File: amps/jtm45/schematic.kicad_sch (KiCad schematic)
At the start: 63 parts, among them T3 OT

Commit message: Add: the 56 pF the JTM45 drawing hangs across the bright-channel mixer
The factory drawing draws a capacitor across the bright channel's 270K
mixer (RM2): top lead on the wiper/270K top, bottom lead on the mixed
node. Its label reads "56pF", the first glyph partly overdrawn by the
lead, so the value is probable rather than certain; the BOM role says so.
Added as C19 on the parts list, sheet and board. AC-only: not in the DC
model.

Co-Authored-By: Claude Opus 5.5 <noreply@anthropic.com>
Claude-Session: https://claude.ai/code/session_01KBMfdh37HmCL2iWcBiL5J1
Signed-off-by: AnalogMaker <theanalogmaker@gmail.com>
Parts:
- removed C5: .02u, symbol cx:C
- removed RK1: 820, symbol cx:R
- removed RL3: 100k, symbol cx:R
- removed RNFB: 27k, symbol cx:R
- removed RSL: 56k, symbol cx:R
- removed RT2: 10k, symbol cx:R
- added C19: 56p, symbol cx:C
- added C4: 270p, symbol cx:C
- added C6: .02u, symbol cx:C
- added RGA: 1M, symbol cx:R
- added V3A: ECC83, symbol cx:TRIODE
- added V3B: ECC83 CF, symbol cx:TRIODE
- added VR6: 5k pres, symbol cx:POT
- C5: renamed from VR4; value 1M bass -> .02u; symbol cx:POT -> cx:C
- RK1: renamed from V3A; value ECC83 -> 820; symbol cx:TRIODE -> cx:R
- RL3: renamed from V3B; value ECC83 CF -> 100k; symbol cx:TRIODE -> cx:R
- RNFB: renamed from VR6; value 5k pres -> 27k; symbol cx:POT -> cx:R
- RSL: renamed from C4; value 270p -> 56k; symbol cx:C -> cx:R
- RT2: renamed from RGA; value 1M -> 10k
- VR4: renamed from C6; value .02u -> 1M bass; symbol cx:C -> cx:POT
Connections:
- net B+4: now also V3B.1 (P)
- net GND: now also RK1.2, VR6.3; no longer RNFB.3
- net PRES: now also RNFB.2, RT2.2, VR6.1; no longer RNFB.1
- net SPKR: now also RNFB.1
- net at RKCF.1, RSL.1: now also C4.1, V3B.3 (K); no longer RL3.3 (K)
- net at RSL.2: now also C5.1, C6.1; no longer VR3.1
- net at VR3.3: now also C5.2, VR4.1; no longer C5.1
- net at RL3.2: now also V3A.1 (P), V3B.2 (G); no longer RK1.1 (P)
- net at RM1.2, RM2.2: now also C19.2, V3A.2 (G); no longer RK1.2 (G)
- net at RK2.1: now also V3A.3 (K); no longer RK1.3 (K)
- net at C3.1, V1A.3 (K), V1B.3 (K): now also RK1.1
- net at C7.2, V4A.2 (G): now also RGA.1; no longer RT2.1
- net at VR5.2 (W): now also C6.2; no longer VR4.2
- net at C17.1: now also VR6.2 (W); no longer RNFB.2 (W)
- net at RGB.1, RTAIL.2: now also RT2.1, RGA.2; no longer RT2.2
- net at RM2.1, VR2.2 (W): now also C19.1
- new net: VR4.2 (W), VR4.3, VR5.1
- new net: C4.2, VR3.1
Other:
- moved on the sheet: RT2
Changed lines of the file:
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@@
   (wire (pts (xy 85.0488 64.988) (xy 85.0488 55.278))
     (stroke (width 0) (type default)))
+  (symbol (lib_id "cx:C") (at 78.6988 70.068 90) (unit 1)
+    (in_bom yes) (on_board yes)
+    (property "Reference" "C19" (at 75.4988 74.268 270) (effects (font (size 1.27 1.27)) (justify left)))
+    (property "Value" "56p" (at 75.4988 76.668 270) (effects (font (size 1.27 1.27)) (justify left))))
+  (wire (pts (xy 74.8888 64.988) (xy 74.8888 70.068))
+    (stroke (width 0) (type default)))
+  (wire (pts (xy 82.5088 64.988) (xy 82.5088 70.068))
+    (stroke (width 0) (type default)))
+  (junction (at 74.8888 64.988) (diameter 1.02) (color 0 0 0 0))
+  (junction (at 82.5088 64.988) (diameter 1.02) (color 0 0 0 0))
   (junction (at 85.0488 55.278) (diameter 1.02) (color 0 0 0 0))
   (text "100 pF bright cap across VR2 omitted (AC only)" (at 51.6088 50.278 0)

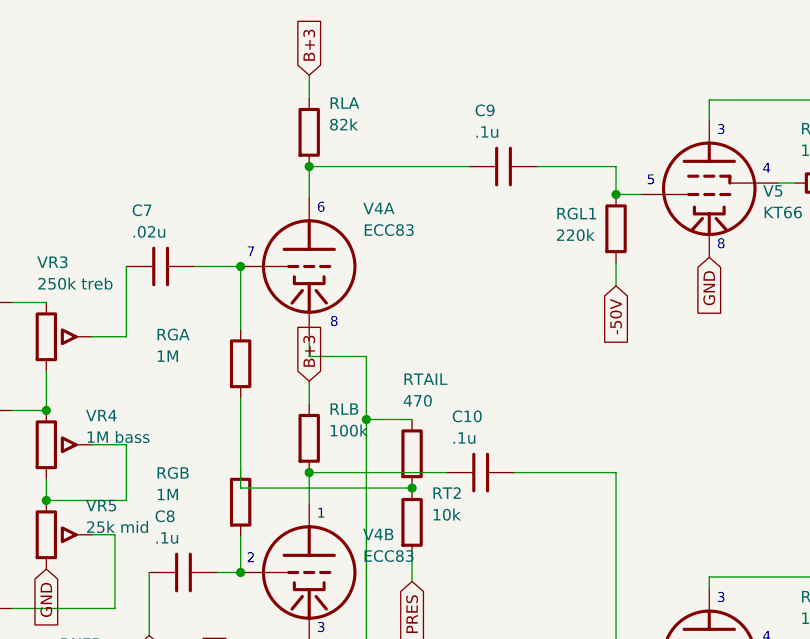
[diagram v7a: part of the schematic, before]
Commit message: Add: the JTM45 phase inverter's plate-to-plate capacitor, value not legible
The factory drawing draws a capacitor between the V4A and V4B plate lines
(junction dots on both). Its value marks match no digit on the drawing,
so it is listed as C20 with "value not legible" and lettered without a
value on the sheet; no placeholder value is invented. DC-open, so it stays
out of the DC model. Added to the parts list, sheet and board.

Co-Authored-By: Claude Opus 5.5 <noreply@anthropic.com>
Claude-Session: https://claude.ai/code/session_01KBMfdh37HmCL2iWcBiL5J1
Signed-off-by: AnalogMaker <theanalogmaker@gmail.com>
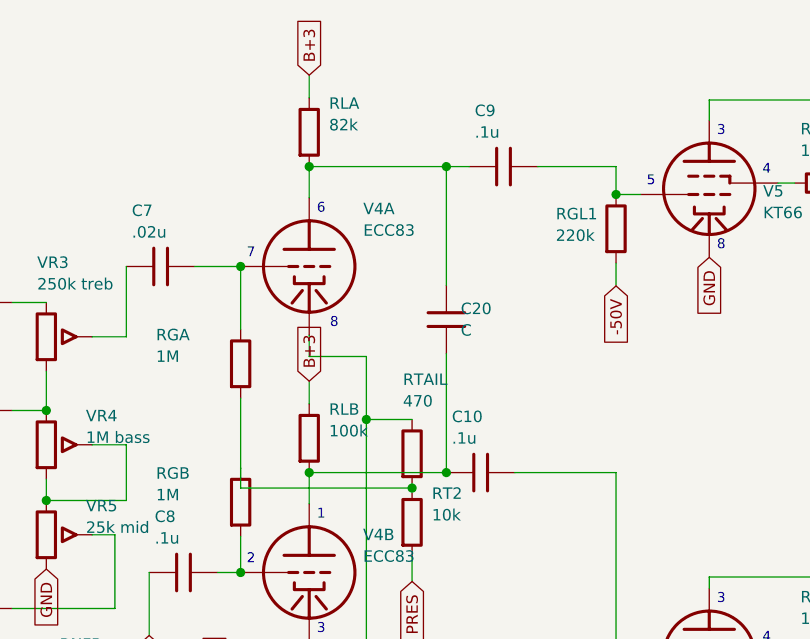
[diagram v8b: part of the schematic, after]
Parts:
- removed C9: .1u, symbol cx:C
- removed RD2: 10k, symbol cx:R
- removed RNFB: 27k, symbol cx:R
- removed RS1: 1k 2W, symbol cx:R
- added C15: .05u, symbol cx:C
- added RGA: 1M, symbol cx:R
- added RGL1, RGL2: 220k, symbol cx:R
- added VR6: 5k pres, symbol cx:POT
- C10: renamed from RGL2; value 220k -> .1u; symbol cx:R -> cx:C
- C14: renamed from RB1; value 150k -> 16u; symbol cx:R -> cx:C
- C20: renamed from RGA; value 1M -> C; symbol cx:R -> cx:C
- C9: renamed from RGL1; value 220k -> .1u; symbol cx:R -> cx:C
- RB1: renamed from C15; value .05u -> 150k; symbol cx:C -> cx:R
- RD2: renamed from C14; value 16u -> 10k; symbol cx:C -> cx:R
- RNFB: renamed from VR6; value 5k pres -> 27k; symbol cx:POT -> cx:R
- RS1: renamed from C10; value .1u -> 1k 2W; symbol cx:C -> cx:R
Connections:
- net -50V: now also RB1.2, C15.1, RGL1.2, RGL2.2; no longer C10.2, C14.2, C9.2, RB1.1
- net B+2: now also RS1.2
- net B+3: now also RD2.1
- net B+4: now also C14.1, RD2.2; no longer RD2.1
- net GND: now also C14.2, C15.2, VR6.3; no longer RB1.2, RD2.2, RNFB.3
- net PRES: now also RNFB.2, VR6.1; no longer RNFB.1
- net SPKR: now also RNFB.1
- net at C9.1: now also C20.1, RLA.2, V4A.1 (P); no longer V5.2 (G1)
- net at V5.3 (G2): now also RS1.1
- net at C7.2, V4A.2 (G): now also RGA.1; no longer C20.1
- net at C17.1: now also VR6.2 (W); no longer RNFB.2 (W)
- net at D1.1 (A): now also RB1.1; no longer C14.1
- net at RGB.1, RT2.1, RTAIL.2: now also RGA.2; no longer C20.2
- net at RLB.2, V4B.1 (P): now also C10.1, C20.2; no longer RS1.1
- new net: C10.2, RGL2.1, V6.2 (G1)
- new net: C9.2, RGL1.1, V5.2 (G1)
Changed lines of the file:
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@@
   (global_label "PRES" (shape input) (at 181.569 73.278 270)
     (effects (font (size 1.27 1.27)) (justify right)))
+  (wire (pts (xy 185.379 27.178) (xy 185.379 40.368))
+    (stroke (width 0) (type default)))
+  (junction (at 185.379 27.178) (diameter 1.02) (color 0 0 0 0))
+  (symbol (lib_id "cx:C") (at 185.379 44.178 0) (unit 1)
+    (in_bom yes) (on_board yes)
+    (property "Reference" "C20" (at 186.979 42.978 0) (effects (font (size 1.27 1.27)) (justify left)))
+    (property "Value" "C" (at 186.979 45.378 0) (effects (font (size 1.27 1.27)) (justify left))))
+  (wire (pts (xy 185.379 47.988) (xy 185.379 61.178))
+    (stroke (width 0) (type default)))
+  (junction (at 185.379 61.178) (diameter 1.02) (color 0 0 0 0))
   (wire (pts (xy 162.519 38.278) (xy 162.519 45.278))
     (stroke (width 0) (type default)))
@@
   (global_label "GND" (shape input) (at 186.609 97.708 270)
     (effects (font (size 1.27 1.27)) (justify right)))
-  (wire (pts (xy 170.139 27.178) (xy 187.919 27.178))
+  (wire (pts (xy 170.139 27.178) (xy 185.379 27.178))
+    (stroke (width 0) (type default)))
+  (wire (pts (xy 185.379 27.178) (xy 187.919 27.178))
     (stroke (width 0) (type default)))
   (junction (at 170.139 27.178) (diameter 1.02) (color 0 0 0 0))
